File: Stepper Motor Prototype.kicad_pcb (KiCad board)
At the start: 4 copper layers, 71 x 79 mm, 39 parts, among them J1 Conn_01x16, J2 Screw_Terminal_01x02, J3 Screw_Terminal_01x04, Q1 STD20NF06L, Q2 STD20NF06L, Q3 STD20NF06L, Q4 STD20NF06L, Q5 STD20NF06L, Q6 STD20NF06L, Q7 STD20NF06L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

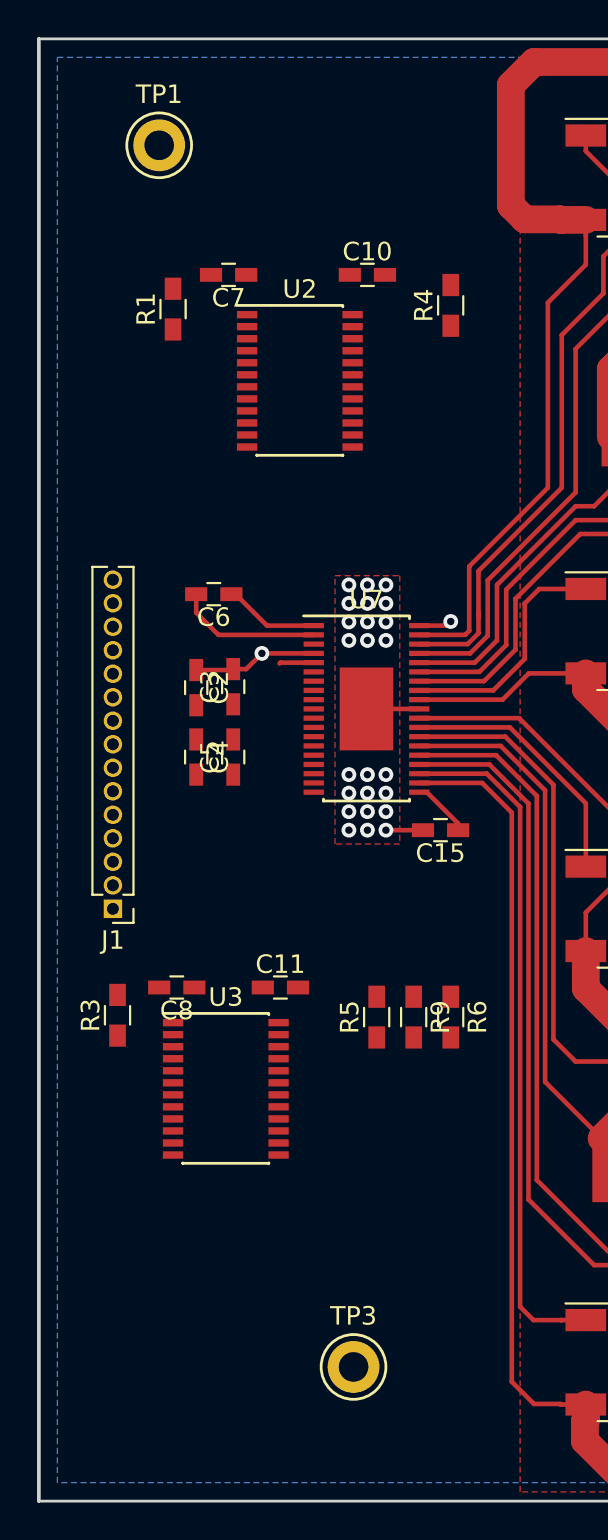
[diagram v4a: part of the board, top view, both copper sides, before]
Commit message: traces are all connected, still need to refine routing of logic side
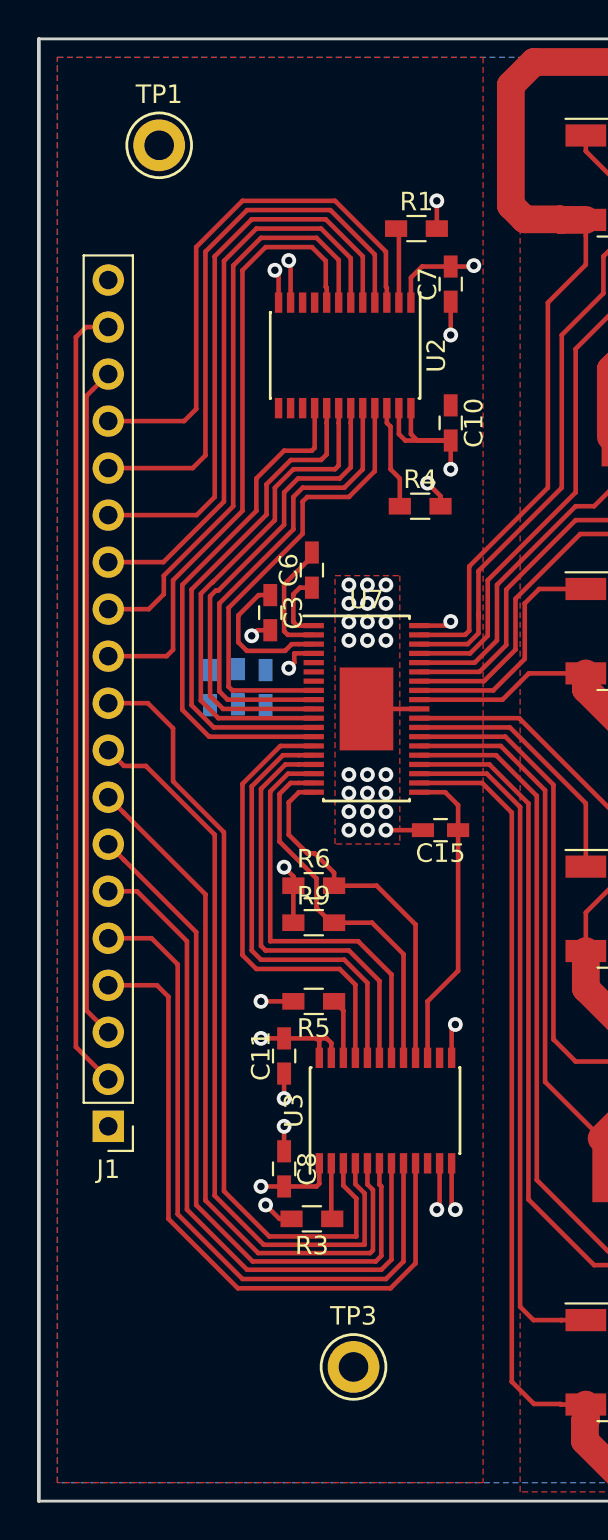
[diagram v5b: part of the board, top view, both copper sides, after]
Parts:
- C2, C4, C5: moved to B.Cu
- J1: value Conn_01x16 -> Conn_01x19; footprint Pin_Headers:Pin_Header_Straight_1x15_Pitch1.27mm -> Pin_Headers:Pin_Header_Straight_1x19_Pitch2.54mm
- moved R3 15.2 mm to (123.8, 113.8), turned to 180 degrees
- moved R1 13.9 mm to (129.4, 60.2), turned to 0 degrees
- moved C7 12.0 mm to (131.2, 63.2), turned to 90 degrees
- moved J1 11.8 mm to (112.8, 108.8)
- moved C8 11.4 mm to (122.2, 111.0), turned to 270 degrees
- moved R4 11.0 mm to (129.6, 75.2), turned to 0 degrees
- moved R6 10.3 mm to (123.8, 95.8), turned to 0 degrees
- moved C10 9.18 mm to (131.2, 70.8), turned to 270 degrees
- moved U3 8.70 mm to (127.7, 107.9), turned to 90 degrees
- moved R9 7.43 mm to (123.8, 97.8), turned to 0 degrees
- moved C6 5.46 mm to (123.8, 78.7), turned to 90 degrees
- moved C3 4.47 mm to (121.5, 81.0), turned to 270 degrees
- moved C4 4.42 mm to (119.8, 85.0)
- moved C5 4.14 mm to (121.2, 85.0), turned to 270 degrees
- moved C11 3.71 mm to (122.2, 105.0), turned to 90 degrees
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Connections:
- J1 pad 2: +1V8 -> +3V3
- J1 pad 3: +3V3 -> +1V8
- U2 pad 3: (no net) -> Net-(J1-Pad16)
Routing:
- net +3V3: track 0.00 -> 58.6 mm, vias 0 -> 6
- net +1V8: track 0.00 -> 55.1 mm, vias 0 -> 3
- net Net-(J1-Pad10): track 0.00 -> 42.6 mm
- net Net-(J1-Pad9): track 0.00 -> 40.9 mm
- net Net-(J1-Pad8): track 0.00 -> 39.1 mm
- net Net-(J1-Pad6): track 0.00 -> 38.2 mm
- net Net-(J1-Pad7): track 0.00 -> 37.9 mm
- net Net-(J1-Pad5): track 0.00 -> 37.2 mm
- net Net-(J1-Pad4): track 0.00 -> 36.4 mm
- net Net-(J1-Pad11): track 0.00 -> 33.3 mm
- net Net-(J1-Pad12): track 0.00 -> 31.8 mm
- net Net-(J1-Pad14): track 0.00 -> 31.3 mm
- net Net-(J1-Pad13): track 0.00 -> 31.2 mm
- net Net-(J1-Pad15): track 0.00 -> 30.2 mm
- net Net-(J1-Pad16): track 0.00 -> 29.0 mm
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- added copper zone on In2.Cu, net +1V8
- added copper zone on In1.Cu, net +3V3

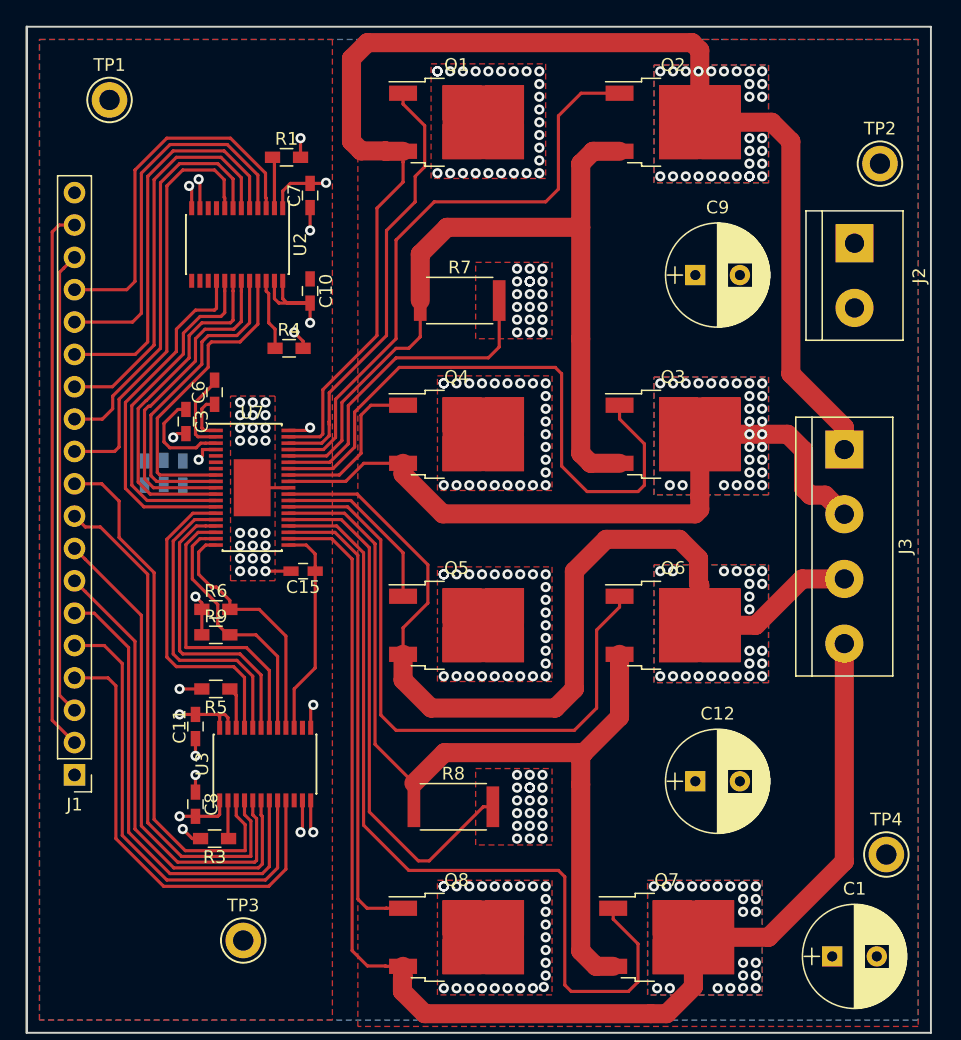
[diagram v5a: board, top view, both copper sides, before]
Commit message: removed voltage level translator, all nets are connected
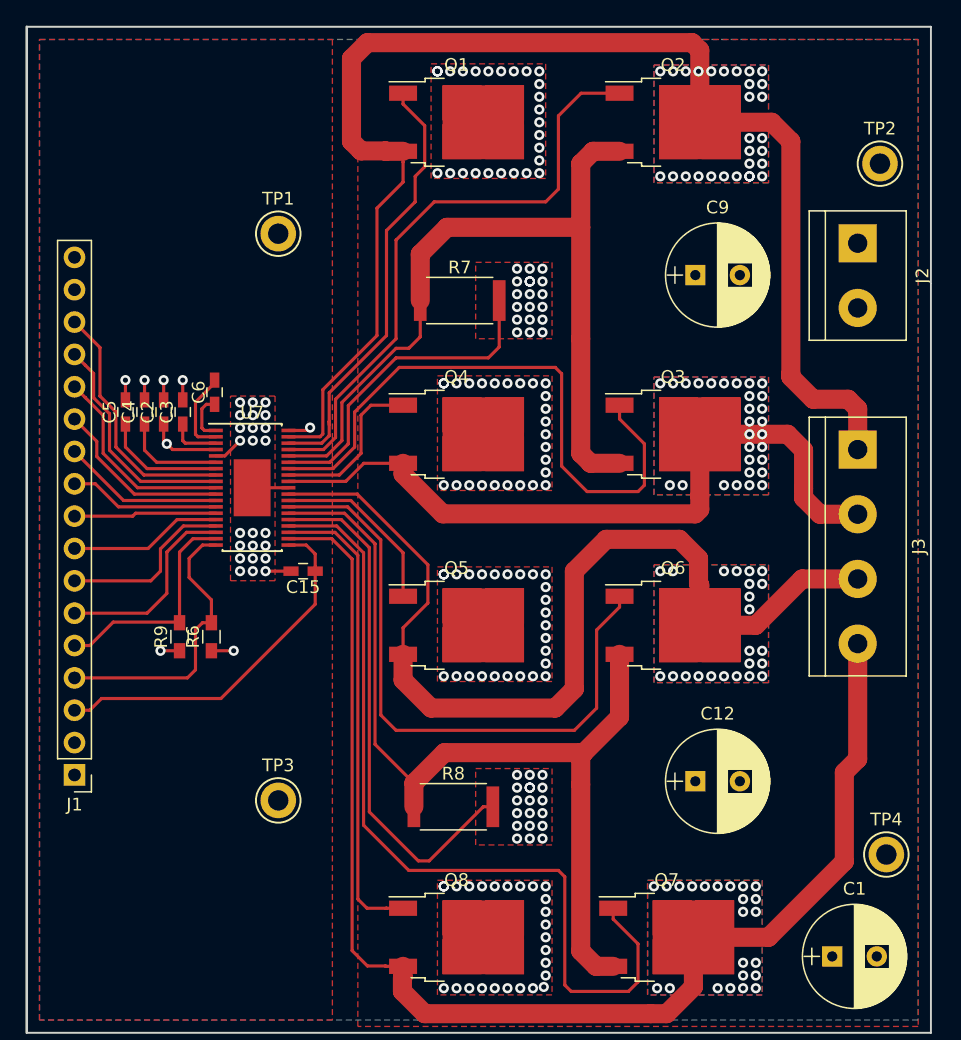
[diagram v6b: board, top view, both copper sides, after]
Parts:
- removed C10, C11, C7, C8: 0.1uF, Capacitors_SMD:C_0603_HandSoldering
- removed R1, R3, R4, R5: 10k, Resistors_SMD:R_0603_HandSoldering
- removed U2, U3: SN74AXC8T245, Housings_SSOP:TSSOP-24_4.4x7.8mm_Pitch0.65mm
- C2, C4, C5: moved to F.Cu
- J1: value Conn_01x19 -> Conn_01x17; footprint Pin_Headers:Pin_Header_Straight_1x19_Pitch2.54mm -> Pin_Headers:Pin_Header_Straight_1x17_Pitch2.54mm
- moved TP1 16.9 mm to (128.8, 66.2)
- moved TP3 11.3 mm to (128.8, 110.8)
- moved C5 6.58 mm to (116.8, 80.2), turned to 90 degrees
- moved C2 5.03 mm to (119.8, 80.2), turned to 90 degrees
- moved C4 4.98 mm to (118.2, 80.2), turned to 90 degrees
- moved R9 2.85 mm to (121.0, 97.9), turned to 90 degrees
- moved R6 2.18 mm to (123.5, 97.9), turned to 90 degrees
- moved J3 1.05 mm to (174.2, 83.2)
- moved C3 0.79 mm to (121.2, 80.2), turned to 90 degrees
- moved J2 0.25 mm to (174.2, 67.0)
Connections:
- J1 pad 16: Net-(J1-Pad16) -> +3V3
- J1 pad 17: +1V8 -> GND
- J1 pad 3: +1V8 -> Net-(C15-Pad1)
- R6 pad 1: +1V8 -> +3V3
- R6 pad 2: Net-(R6-Pad2) -> Net-(J1-Pad4)
- R9 pad 1: +1V8 -> +3V3
- R9 pad 2: Net-(R9-Pad2) -> Net-(J1-Pad5)
- U7 pad 10: Net-(U2-Pad19) -> Net-(J1-Pad13)
- U7 pad 11: Net-(U2-Pad18) -> Net-(J1-Pad12)
- U7 pad 12: Net-(U2-Pad17) -> Net-(J1-Pad11)
- U7 pad 13: Net-(U2-Pad16) -> Net-(J1-Pad10)
- U7 pad 14: Net-(U3-Pad21) -> Net-(J1-Pad9)
- U7 pad 15: Net-(U3-Pad20) -> Net-(J1-Pad8)
- U7 pad 16: Net-(U3-Pad19) -> Net-(J1-Pad7)
- U7 pad 17: Net-(U3-Pad18) -> Net-(J1-Pad6)
- U7 pad 18: Net-(R9-Pad2) -> Net-(J1-Pad5)
- U7 pad 19: Net-(R6-Pad2) -> Net-(J1-Pad4)
- U7 pad 8: Net-(U2-Pad21) -> Net-(J1-Pad15)
- U7 pad 9: Net-(U2-Pad20) -> Net-(J1-Pad14)
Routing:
- net +3V3: track 58.6 -> 3.25 mm, vias 6 -> 2
- net +1V8: track 55.1 -> 0.00 mm, vias 3 -> 0
- net Net-(J1-Pad10): track 42.6 -> 11.8 mm
- net Net-(J1-Pad9): track 40.9 -> 11.2 mm
- net Net-(J1-Pad16): track 29.0 -> 0.00 mm
- net Net-(U2-Pad16): track 27.8 -> 0.00 mm
- net Net-(U2-Pad17): track 27.1 -> 0.00 mm
- net Net-(J1-Pad8): track 39.1 -> 12.0 mm
- net Net-(U2-Pad18): track 26.7 -> 0.00 mm
- net Net-(U2-Pad19): track 26.0 -> 0.00 mm
- net Net-(U2-Pad20): track 25.1 -> 0.00 mm
- net Net-(U3-Pad21): track 24.7 -> 0.00 mm
- net Net-(U2-Pad21): track 24.3 -> 0.00 mm
- net Net-(J1-Pad7): track 37.9 -> 13.9 mm
- net Net-(U3-Pad20): track 23.9 -> 0.00 mm
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- removed copper zone on In2.Cu, net +1V8
